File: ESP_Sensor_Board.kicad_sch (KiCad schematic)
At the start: 34 parts, among them J1 USB_B_Micro, Q1 Q_NPN_BEC, Q2 Q_NPN_BEC, Q3 Q_NPN_BEC, U1 LMR62421XMF, U2 ESP32-WROOM-32D, U3 CH340C, U4 LM75B, U5 HP203B, Y1 32.768kHz

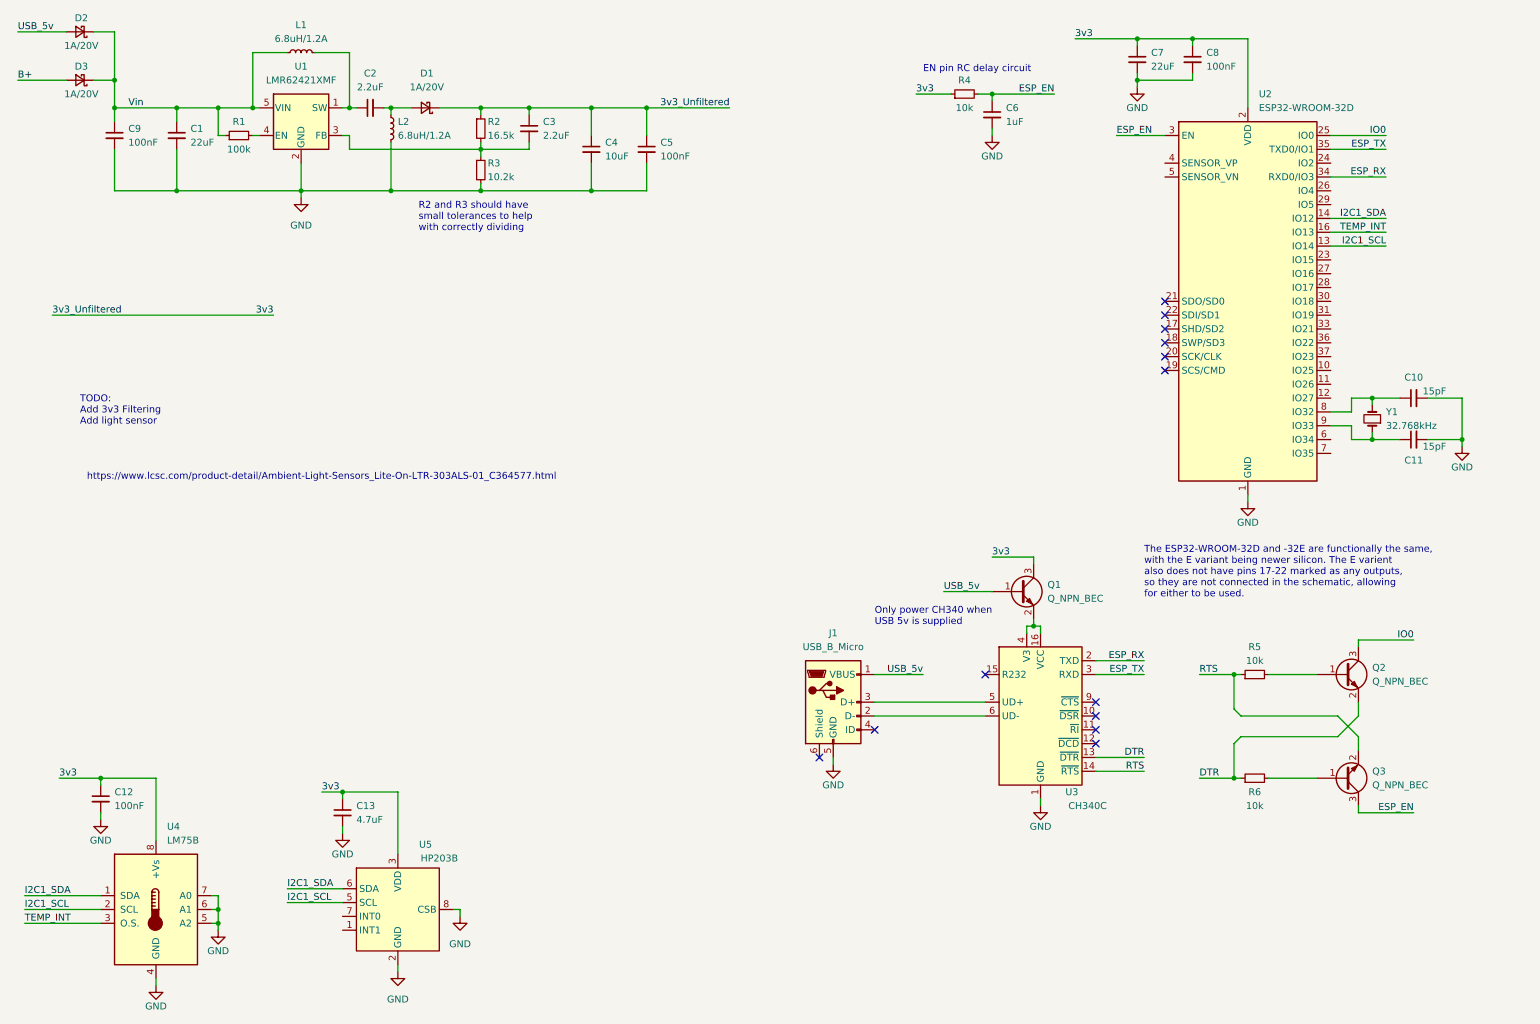
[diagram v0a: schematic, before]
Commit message: Started work adding voltage divider
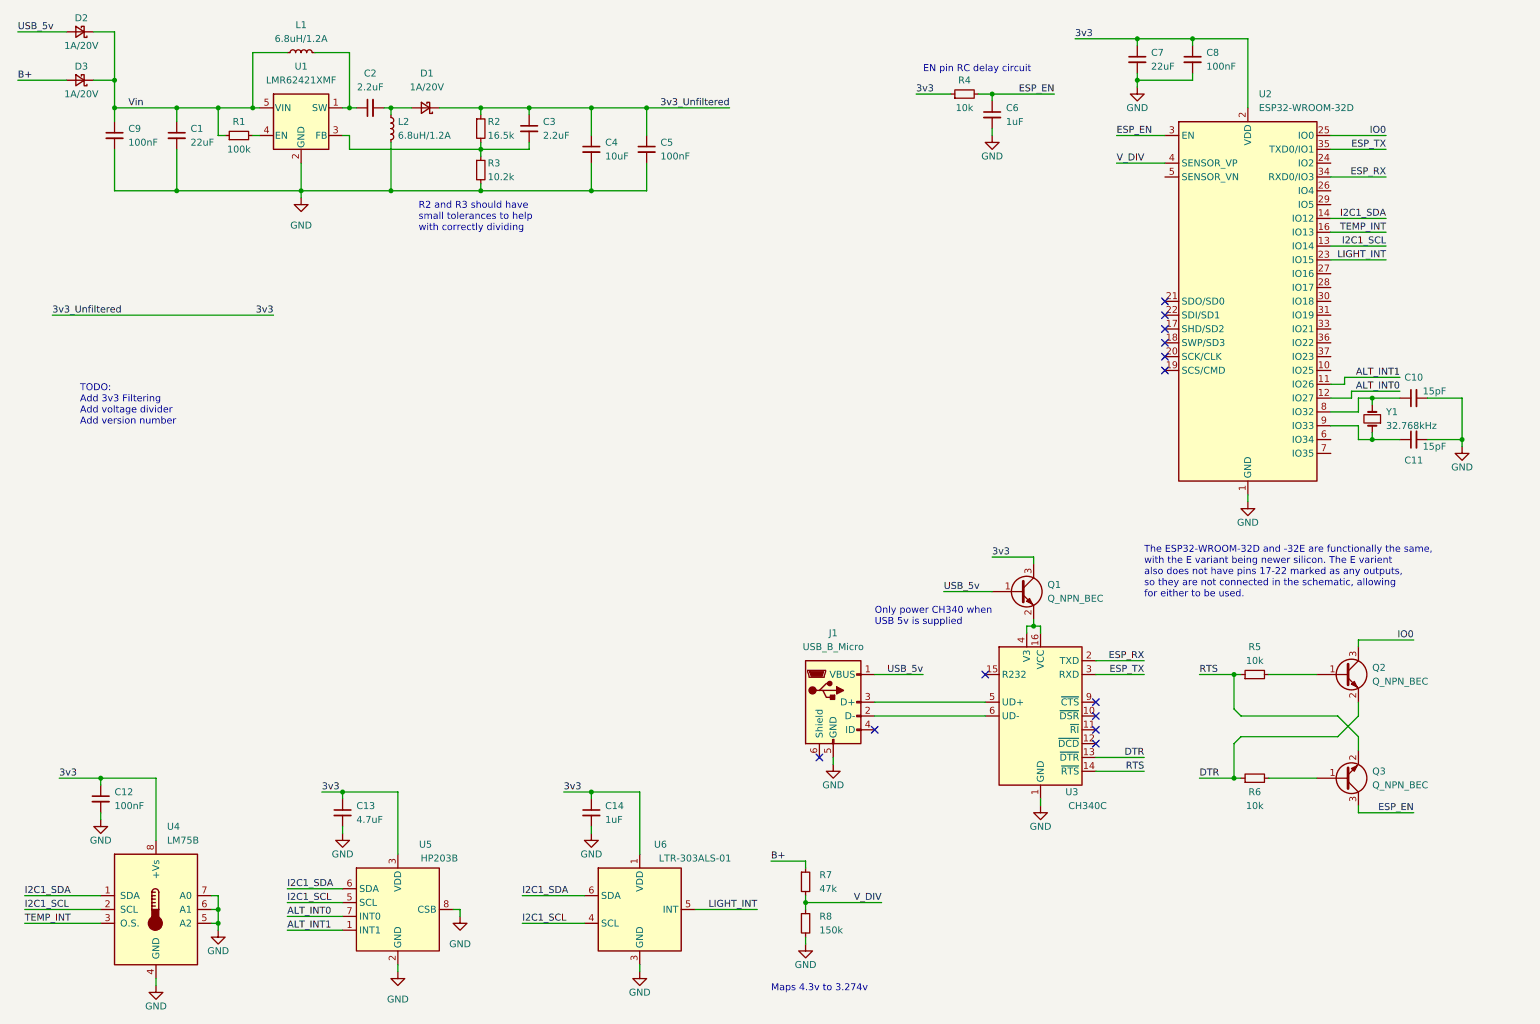
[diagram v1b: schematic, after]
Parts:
- added C14: 1uF, Capacitor_SMD:C_0603_1608Metric, symbol Device:C_Small
- added R7: 47k, Resistor_SMD:R_0603_1608Metric, symbol Device:R_Small
- added R8: 150k, Resistor_SMD:R_0603_1608Metric, symbol Device:R_Small
- added U6: LTR-303ALS-01, OptoDevice:Lite-On_LTR-303ALS-01, symbol Sensor_Optical:LTR-303ALS-01
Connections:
- net 3v3: now also C14.1, U6.1 (VDD)
- net B+: now also R7.1
- net GND: now also C14.2, R8.2, U6.3 (GND)
- net I2C1_SCL: now also U6.4 (SCL)
- net I2C1_SDA: now also U6.6 (SDA)
- net ALT_INT1: now reaches U5.1 (INT1)
- net ALT_INT1: now also U2.11 (IO26)
- net ALT_INT0: now reaches U5.7 (INT0)
- net ALT_INT0: now also U2.12 (IO27)
- net LIGHT_INT: now reaches U2.23 (IO15)
- net LIGHT_INT: now also U6.5 (INT)
- net V_DIV: now reaches U2.4 (SENSOR_VP)
- net V_DIV: now also R7.2, R8.1
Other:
- note added: "Maps 4.3v to 3.274v"
- note added: "TODO: Add 3v3 Filtering Add voltage divider Add version number"
- note removed: "TODO: Add 3v3 Filtering Add light sensor"
- note removed: "https://www.lcsc.com/product-detail/Ambient-Light-Sensors_Lite-On-LTR-303ALS-01_C364577.html"

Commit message: Moved sensors to back of board, added battery pads
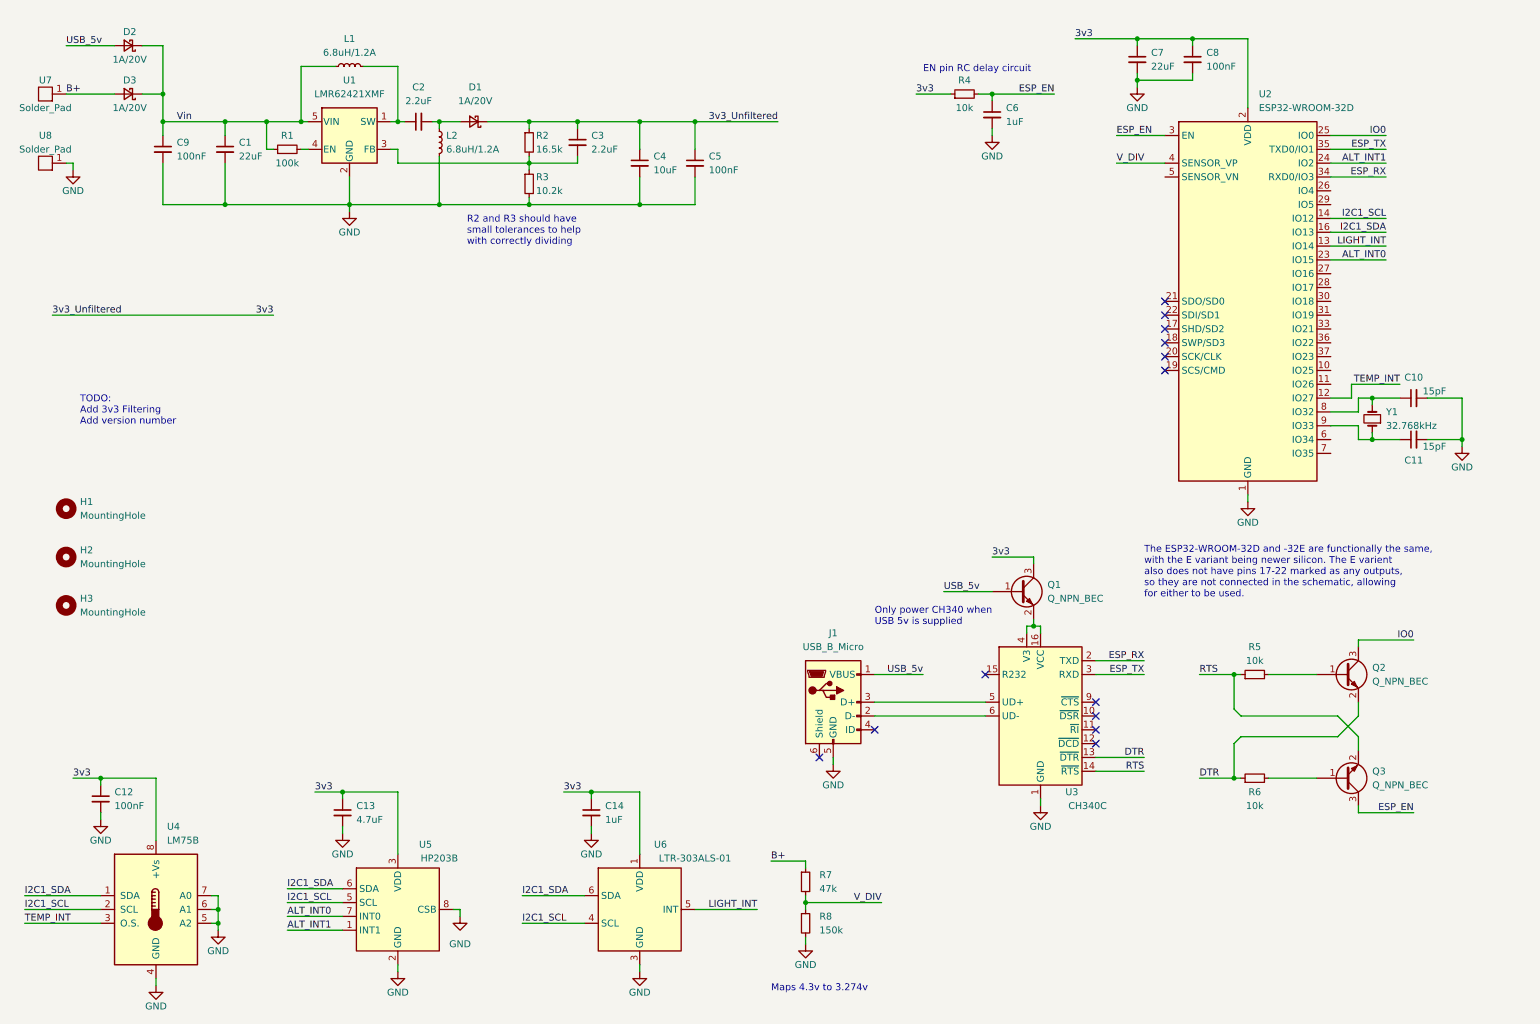
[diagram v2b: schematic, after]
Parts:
- added H1, H2, H3: MountingHole, MountingHole:MountingHole_3.2mm_M3, symbol Mechanical:MountingHole
- added U7, U8: Solder_Pad, ESP_Sensor_Board:Pad, symbol ESP_Sensor_Board:Solder_Pad
- C14: LCSC Part Number (none) -> C1592; Manufacturer (none) -> Samsung Electro-Mechanics; Manufacturer Part Number (none) -> CL10A105KO8NNNC
- U6: LCSC Part Number (none) -> C364577; Manufacturer (none) -> Lite-On; Manufacturer Part Number (none) -> LTR-303ALS-01
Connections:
- net ALT_INT0: now also U2.23 (IO15); no longer U2.12 (IO27)
- net ALT_INT1: now also U2.24 (IO2); no longer U2.11 (IO26)
- net B+: now also U7.1
- net GND: now also U8.1
- net I2C1_SCL: now also U2.14 (IO12); no longer U2.13 (IO14)
- net I2C1_SDA: now also U2.16 (IO13); no longer U2.14 (IO12)
- net LIGHT_INT: now also U2.13 (IO14); no longer U2.23 (IO15)
- net TEMP_INT: now also U2.12 (IO27); no longer U2.16 (IO13)
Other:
- note added: "TODO: Add 3v3 Filtering Add version number"
- note removed: "TODO: Add 3v3 Filtering Add voltage divider Add version number"
- moved on the sheet: C1, C2, C3, C4, C5, C9, D1, D2, D3, L1, L2, R1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
